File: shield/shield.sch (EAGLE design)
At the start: 23 parts, among them IC1 MCP2515-E/SO, IC2 MCP2551, IC3 LM2595NDH

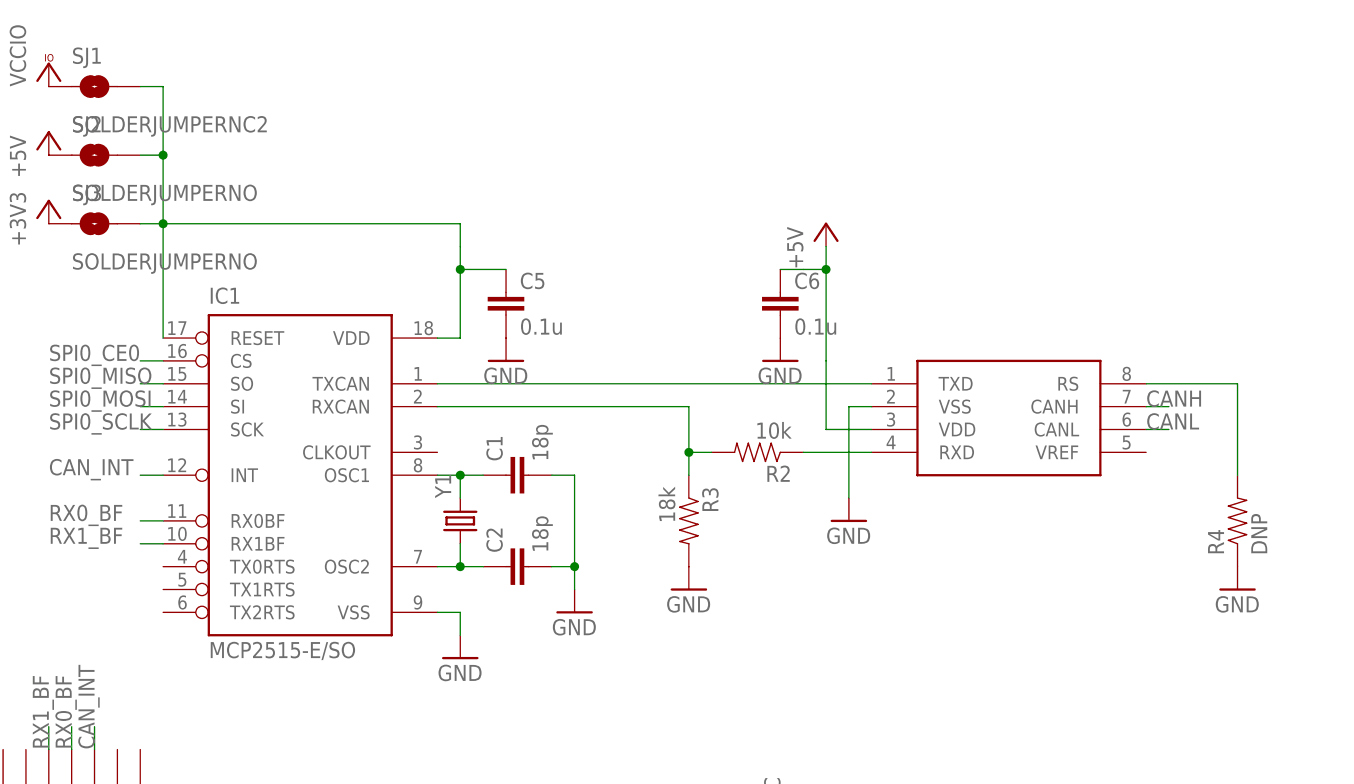
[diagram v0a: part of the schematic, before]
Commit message: Added power injector board; refactored boards to use MCP2562 instead of MCP2551
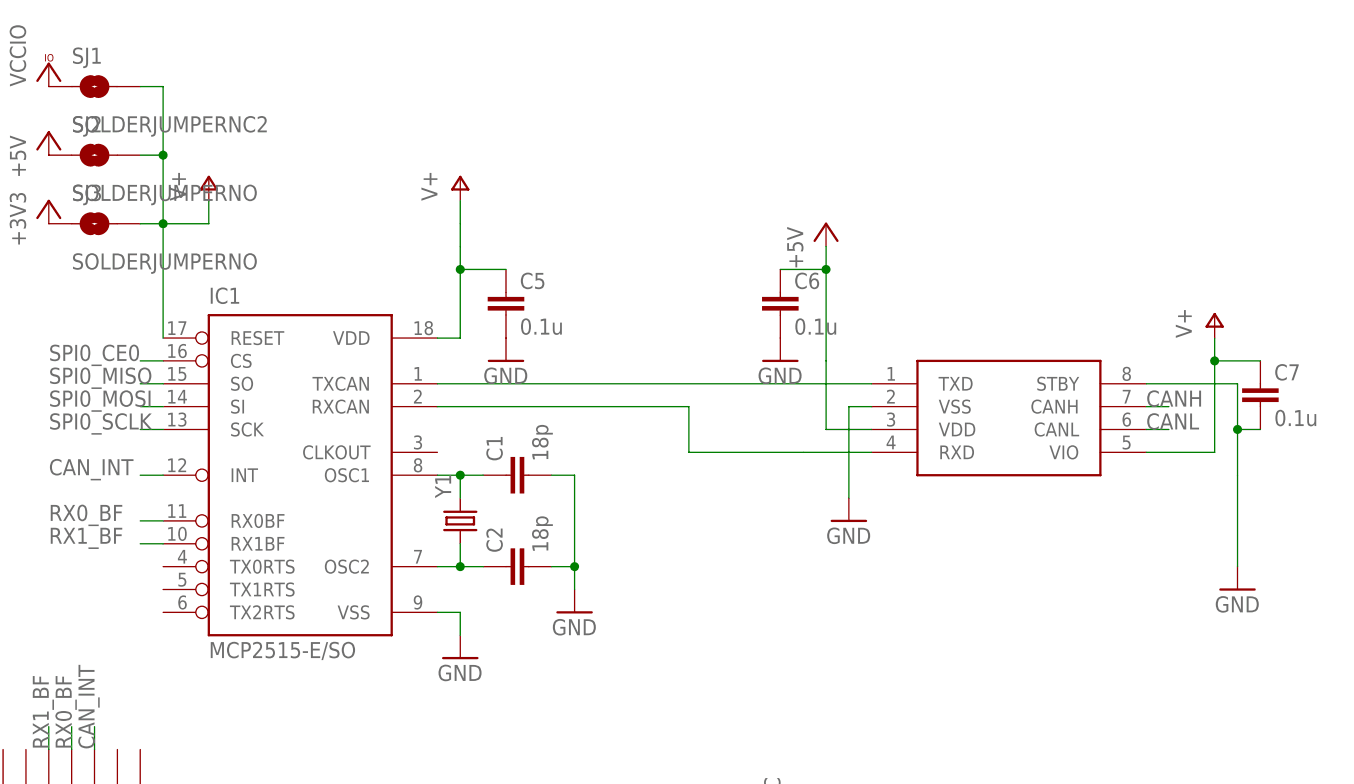
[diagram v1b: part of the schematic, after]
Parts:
- removed R2: 10k, SparkFun-Passives:RESISTOR0603-RES
- removed R3: 18k, SparkFun-Passives:RESISTOR0603-RES
- removed R4: DNP, SparkFun-Passives:RESISTOR0603-RES
- added C7: 0.1u, SparkFun-Passives:CAP0603-CAP
- IC2: value MCP2551 -> MCP2562; device SparkFun-DigitalIC:MCP2551 -> nickparts:MCP2562
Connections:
- removed net N$2: IC1.RXCAN, R2.2, R3.1
- removed net N$3: C5.1, IC1.RESET, IC1.VDD, SJ1.2, SJ2.2, SJ3.2
- removed net N$8: IC2.RS, R4.2
- new net V+: C5.1, C7.1, IC1.RESET, IC1.VDD, IC2.VIO, SJ1.2, SJ2.2, SJ3.2
- net GND: now also C7.2, IC2.STBY; no longer R3.2, R4.1
- net N$1: now also IC1.RXCAN; no longer R2.1
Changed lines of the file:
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@@
 <part name="D1" library="SparkFun-DiscreteSemi" deviceset="DIODE" device="SMA-ALT"/>
 <part name="IC1" library="mcp2515" deviceset="MCP2515" device="-E/SO"/>
-<part name="IC2" library="SparkFun-DigitalIC" deviceset="MCP2551" device=""/>
+<part name="IC2" library="nickparts" deviceset="MCP2562" device=""/>
 <part name="GND3" library="supply1" deviceset="GND" device=""/>
 <part name="P+1" library="supply1" deviceset="+5V" device=""/>
@@
 <part name="GND9" library="supply1" deviceset="GND" device=""/>
 <part name="GND10" library="supply1" deviceset="GND" device=""/>
-<part name="R4" library="SparkFun-Passives" deviceset="RESISTOR" device="0603-RES" value="DNP"/>
 <part name="GND11" library="supply1" deviceset="GND" device=""/>
 <part name="U$1" library="adafruit" deviceset="ARDUINO_R3_ICSP" device=""/>
@@
 <part name="VCC1" library="supply1" deviceset="VCCIO" device=""/>
 <part name="VCC3" library="supply1" deviceset="VCCIO" device=""/>
-<part name="R2" library="SparkFun-Passives" deviceset="RESISTOR" device="0603-RES" value="10k"/>
-<part name="R3" library="SparkFun-Passives" deviceset="RESISTOR" device="0603-RES" value="18k"/>
-<part name="GND1" library="supply1" deviceset="GND" device=""/>
 <part name="P+6" library="supply1" deviceset="+5V" device=""/>
 <part name="SJ1" library="SparkFun-Passives" deviceset="SOLDERJUMPER" device="NC2"/>
@@
 <part name="+3V1" library="supply1" deviceset="+3V3" device=""/>
 <part name="+3V2" library="supply1" deviceset="+3V3" device=""/>
+<part name="P+7" library="supply1" deviceset="V+" device=""/>
+<part name="P+8" library="supply1" deviceset="V+" device=""/>
+<part name="C7" library="SparkFun-Passives" deviceset="CAP" device="0603-CAP" value="0.1u"/>
+<part name="P+9" library="supply1" deviceset="V+" device=""/>
 </parts>
 <sheets>
@@
 <instance part="GND9" gate="1" x="368.3" y="-17.78"/>
 <instance part="GND10" gate="1" x="337.82" y="-17.78"/>
-<instance part="R4" gate="G$1" x="419.1" y="-35.56" rot="R90"/>
 <instance part="GND11" gate="1" x="419.1" y="-43.18"/>
 <instance part="U$1" gate="G$1" x="243.84" y="-116.84"/>
@@
 <instance part="VCC1" gate="G$1" x="259.08" y="-121.92"/>
 <instance part="VCC3" gate="G$1" x="287.02" y="15.24"/>
-<instance part="R2" gate="G$1" x="365.76" y="-27.94" rot="R180"/>
-<instance part="R3" gate="G$1" x="358.14" y="-35.56" rot="R270"/>
-<instance part="GND1" gate="1" x="358.14" y="-43.18"/>
 <instance part="P+6" gate="1" x="304.8" y="-83.82"/>
 <instance part="SJ1" gate="1" x="292.1" y="12.7"/>
@@
 <instance part="+3V1" gate="G$1" x="287.02" y="0"/>
 <instance part="+3V2" gate="G$1" x="251.46" y="-121.92"/>
+<instance part="P+7" gate="1" x="304.8" y="2.54"/>
+<instance part="P+8" gate="1" x="332.74" y="2.54"/>
+<instance part="C7" gate="G$1" x="421.64" y="-22.86"/>
+<instance part="P+9" gate="1" x="416.56" y="-12.7"/>
 </instances>
 <busses>
@@
 <pinref part="C5" gate="G$1" pin="2"/>
 <pinref part="GND10" gate="1" pin="GND"/>
-</segment>
-<segment>
-<pinref part="R4" gate="G$1" pin="1"/>
-<pinref part="GND11" gate="1" pin="GND"/>
 </segment>
 <segment>
@@
 </segment>
 <segment>
-<pinref part="R3" gate="G$1" pin="2"/>
-<pinref part="GND1" gate="1" pin="GND"/>
+<pinref part="IC2" gate="G$1" pin="STBY"/>
+<wire x1="408.94" y1="-20.32" x2="419.1" y2="-20.32" width="0.1524" layer="91"/>
+<wire x1="419.1" y1="-20.32" x2="419.1" y2="-25.4" width="0.1524" layer="91"/>
+<pinref part="GND11" gate="1" pin="GND"/>
+<wire x1="419.1" y1="-25.4" x2="419.1" y2="-30.48" width="0.1524" layer="91"/>
+<wire x1="419.1" y1="-30.48" x2="419.1" y2="-40.64" width="0.1524" layer="91"/>
+<pinref part="C7" gate="G$1" pin="2"/>
+<wire x1="421.64" y1="-25.4" x2="419.1" y2="-25.4" width="0.1524" layer="91"/>
+<junction x="419.1" y="-25.4"/>
 </segment>
 </net>
@@
 </segment>
 </net>
-<net name="N$8" class="0">
-<segment>
-<pinref part="IC2" gate="G$1" pin="RS"/>
-<pinref part="R4" gate="G$1" pin="2"/>
-<wire x1="408.94" y1="-20.32" x2="419.1" y2="-20.32" width="0.1524" layer="91"/>
-<wire x1="419.1" y1="-20.32" x2="419.1" y2="-30.48" width="0.1524" layer="91"/>
-</segment>
-</net>
 <net name="N$10" class="0">
 <segment>
@@
 <segment>
 <pinref part="IC2" gate="G$1" pin="RXD"/>
-<pinref part="R2" gate="G$1" pin="1"/>
 <wire x1="378.46" y1="-27.94" x2="370.84" y2="-27.94" width="0.1524" layer="91"/>
-</segment>
-</net>
-<net name="N$2" class="0">
-<segment>
-<pinref part="R2" gate="G$1" pin="2"/>
-<pinref part="R3" gate="G$1" pin="1"/>
-<wire x1="360.68" y1="-27.94" x2="358.14" y2="-27.94" width="0.1524" layer="91"/>
-<wire x1="358.14" y1="-27.94" x2="358.14" y2="-30.48" width="0.1524" layer="91"/>
 <pinref part="IC1" gate="G$1" pin="RXCAN"/>
 <wire x1="330.2" y1="-22.86" x2="358.14" y2="-22.86" width="0.1524" layer="91"/>
-<wire x1="358.14" y1="-22.86" x2="358.14" y2="-27.94" width="0.1524" layer="91"/>
-<junction x="358.14" y="-27.94"/>
-</segment>
-</net>
-<net name="N$3" class="0">
-<segment>
-<pinref part="IC1" gate="G$1" pin="VDD"/>
-<wire x1="330.2" y1="-15.24" x2="332.74" y2="-15.24" width="0.1524" layer="91"/>
-<wire x1="332.74" y1="-15.24" x2="332.74" y2="-7.62" width="0.1524" layer="91"/>
-<pinref part="C5" gate="G$1" pin="1"/>
-<wire x1="337.82" y1="-7.62" x2="332.74" y2="-7.62" width="0.1524" layer="91"/>
-<wire x1="332.74" y1="-7.62" x2="332.74" y2="-5.08" width="0.1524" layer="91"/>
-<junction x="332.74" y="-7.62"/>
-<wire x1="332.74" y1="-5.08" x2="332.74" y2="-2.54" width="0.1524" layer="91"/>
+<wire x1="370.84" y1="-27.94" x2="358.14" y2="-27.94" width="0.1524" layer="91"/>
+<wire x1="358.14" y1="-27.94" x2="358.14" y2="-22.86" width="0.1524" layer="91"/>
+</segment>
+</net>
+<net name="+3V3" class="0">
+<segment>
+<pinref part="SJ3" gate="1" pin="1"/>
+<pinref part="+3V1" gate="G$1" pin="+3V3"/>
+</segment>
+<segment>
+<pinref part="U$1" gate="G$1" pin="3V"/>
+<wire x1="271.78" y1="-121.92" x2="271.78" y2="-129.54" width="0.1524" layer="91"/>
+<pinref part="+3V2" gate="G$1" pin="+3V3"/>
+<wire x1="271.78" y1="-129.54" x2="251.46" y2="-129.54" width="0.1524" layer="91"/>
+<wire x1="251.46" y1="-129.54" x2="251.46" y2="-124.46" width="0.1524" layer="91"/>
+</segment>
+</net>
+<net name="V+" class="0">
+<segment>
 <pinref part="SJ1" gate="1" pin="2"/>
 <wire x1="297.18" y1="12.7" x2="299.72" y2="12.7" width="0.1524" layer="91"/>
@@
 <wire x1="297.18" y1="5.08" x2="299.72" y2="5.08" width="0.1524" layer="91"/>
 <junction x="299.72" y="5.08"/>
-<wire x1="332.74" y1="-2.54" x2="299.72" y2="-2.54" width="0.1524" layer="91"/>
 <junction x="299.72" y="-2.54"/>
 <pinref part="IC1" gate="G$1" pin="RESET"/>
 <wire x1="299.72" y1="-2.54" x2="299.72" y2="-15.24" width="0.1524" layer="91"/>
-</segment>
-</net>
-<net name="+3V3" class="0">
-<segment>
-<pinref part="SJ3" gate="1" pin="1"/>
-<pinref part="+3V1" gate="G$1" pin="+3V3"/>
-</segment>
-<segment>
-<pinref part="U$1" gate="G$1" pin="3V"/>
-<wire x1="271.78" y1="-121.92" x2="271.78" y2="-129.54" width="0.1524" layer="91"/>
-<pinref part="+3V2" gate="G$1" pin="+3V3"/>
-<wire x1="271.78" y1="-129.54" x2="251.46" y2="-129.54" width="0.1524" layer="91"/>
-<wire x1="251.46" y1="-129.54" x2="251.46" y2="-124.46" width="0.1524" layer="91"/>
-</segment>
-</net>
+<pinref part="P+7" gate="1" pin="V+"/>
+<wire x1="299.72" y1="-2.54" x2="304.8" y2="-2.54" width="0.1524" layer="91"/>
+<wire x1="304.8" y1="-2.54" x2="304.8" y2="0" width="0.1524" layer="91"/>
+</segment>
+<segment>
+<wire x1="332.74" y1="-5.08" x2="332.74" y2="-2.54" width="0.1524" layer="91"/>
+<pinref part="C5" gate="G$1" pin="1"/>
+<wire x1="337.82" y1="-7.62" x2="332.74" y2="-7.62" width="0.1524" layer="91"/>
+<wire x1="332.74" y1="-7.62" x2="332.74" y2="-5.08" width="0.1524" layer="91"/>
+<junction x="332.74" y="-7.62"/>
+<wire x1="332.74" y1="-15.24" x2="332.74" y2="-7.62" width="0.1524" layer="91"/>
+<pinref part="IC1" gate="G$1" pin="VDD"/>
+<wire x1="330.2" y1="-15.24" x2="332.74" y2="-15.24" width="0.1524" layer="91"/>
+<pinref part="P+8" gate="1" pin="V+"/>
+<wire x1="332.74" y1="0" x2="332.74" y2="-2.54" width="0.1524" layer="91"/>
+</segment>
+<segment>
+<pinref part="IC2" gate="G$1" pin="VIO"/>
+<wire x1="408.94" y1="-27.94" x2="416.56" y2="-27.94" width="0.1524" layer="91"/>
+<wire x1="416.56" y1="-27.94" x2="416.56" y2="-17.78" width="0.1524" layer="91"/>
+<pinref part="C7" gate="G$1" pin="1"/>
+<wire x1="416.56" y1="-17.78" x2="416.56" y2="-15.24" width="0.1524" layer="91"/>
+<wire x1="421.64" y1="-17.78" x2="416.56" y2="-17.78" width="0.1524" layer="91"/>
+<junction x="416.56" y="-17.78"/>
+<pinref part="P+9" gate="1" pin="V+"/>
+</segment>
+</net>

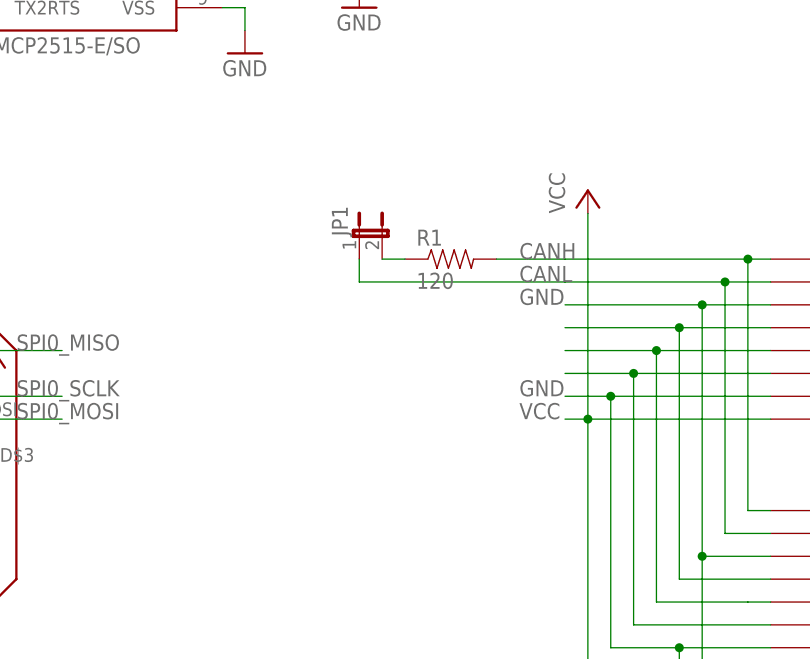
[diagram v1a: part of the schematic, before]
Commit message: Switch to split termination with a switch
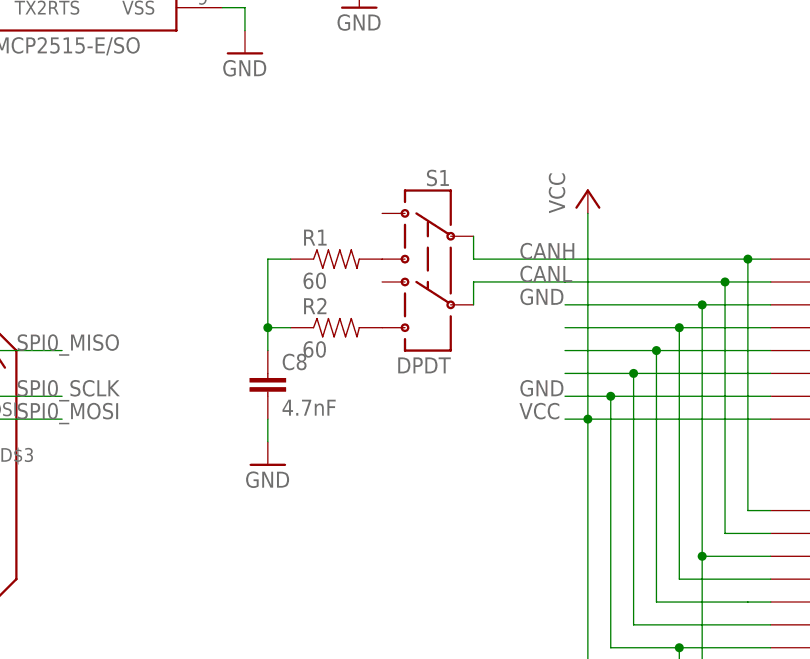
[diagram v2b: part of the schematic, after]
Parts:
- removed JP1: (no value), SparkFun-Passives:JUMPER-2PTH
- added C8: 4.7nF, SparkFun-Passives:CAP0603-CAP
- added R2: 60, SparkFun-Passives:RESISTOR0603-RES
- added S1: DPDT, SparkFun-Electromechanical:SWITCH-DPDTAYZ0202
- R1: value 120 -> 60
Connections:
- new net N$2: R1.2, S1.3
- new net N$3: R2.2, S1.6
- net CANH: now also S1.2; no longer R1.2
- net CANL: now also S1.5; no longer JP1.1
- net GND: now also C8.2
- net N$7: now also C8.1, R2.1; no longer JP1.2
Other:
- moved on the sheet: R1
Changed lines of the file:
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@@
 <part name="GND8" library="supply1" deviceset="GND" device=""/>
 <part name="P+5" library="supply1" deviceset="VCC" device=""/>
-<part name="JP1" library="SparkFun-Passives" deviceset="JUMPER-2" device="PTH"/>
-<part name="R1" library="SparkFun-Passives" deviceset="RESISTOR" device="0603-RES" value="120"/>
+<part name="R1" library="SparkFun-Passives" deviceset="RESISTOR" device="0603-RES" value="60"/>
 <part name="VCC1" library="supply1" deviceset="VCCIO" device=""/>
 <part name="VCC3" library="supply1" deviceset="VCCIO" device=""/>
@@
 <part name="C7" library="SparkFun-Passives" deviceset="CAP" device="0603-CAP" value="0.1u"/>
 <part name="P+9" library="supply1" deviceset="V+" device=""/>
+<part name="S1" library="SparkFun-Electromechanical" deviceset="SWITCH-DPDT" device="AYZ0202" value="DPDT"/>
+<part name="R2" library="SparkFun-Passives" deviceset="RESISTOR" device="0603-RES" value="60"/>
+<part name="C8" library="SparkFun-Passives" deviceset="CAP" device="0603-CAP" value="4.7nF"/>
+<part name="GND1" library="supply1" deviceset="GND" device=""/>
 </parts>
 <sheets>
@@
 <instance part="GND8" gate="1" x="383.54" y="-127"/>
 <instance part="P+5" gate="VCC" x="370.84" y="-66.04"/>
-<instance part="JP1" gate="A" x="345.44" y="-71.12"/>
-<instance part="R1" gate="G$1" x="355.6" y="-73.66"/>
+<instance part="R1" gate="G$1" x="342.9" y="-73.66"/>
 <instance part="VCC1" gate="G$1" x="259.08" y="-121.92"/>
 <instance part="VCC3" gate="G$1" x="287.02" y="15.24"/>
@@
 <instance part="C7" gate="G$1" x="421.64" y="-22.86"/>
 <instance part="P+9" gate="1" x="416.56" y="-12.7"/>
+<instance part="S1" gate="G$1" x="353.06" y="-73.66" rot="MR0"/>
+<instance part="R2" gate="G$1" x="342.9" y="-81.28"/>
+<instance part="C8" gate="G$1" x="335.28" y="-88.9"/>
+<instance part="GND1" gate="1" x="335.28" y="-96.52"/>
 </instances>
 <busses>
@@
 <junction x="419.1" y="-25.4"/>
 </segment>
+<segment>
+<pinref part="C8" gate="G$1" pin="2"/>
+<pinref part="GND1" gate="1" pin="GND"/>
+<wire x1="335.28" y1="-91.44" x2="335.28" y2="-93.98" width="0.1524" layer="91"/>
+</segment>
 </net>
 <net name="N$6" class="0">
@@
 <junction x="388.62" y="-73.66"/>
 <label x="363.22" y="-73.66" size="1.778" layer="95"/>
-<pinref part="R1" gate="G$1" pin="2"/>
-<wire x1="368.3" y1="-73.66" x2="360.68" y2="-73.66" width="0.1524" layer="91"/>
+<pinref part="S1" gate="G$1" pin="2"/>
+<wire x1="368.3" y1="-73.66" x2="358.14" y2="-73.66" width="0.1524" layer="91"/>
+<wire x1="358.14" y1="-73.66" x2="358.14" y2="-71.12" width="0.1524" layer="91"/>
 </segment>
 </net>
@@
 <junction x="386.08" y="-76.2"/>
 <label x="363.22" y="-76.2" size="1.778" layer="95"/>
-<pinref part="JP1" gate="A" pin="1"/>
-<wire x1="368.3" y1="-76.2" x2="345.44" y2="-76.2" width="0.1524" layer="91"/>
-<wire x1="345.44" y1="-76.2" x2="345.44" y2="-73.66" width="0.1524" layer="91"/>
+<pinref part="S1" gate="G$1" pin="5"/>
+<wire x1="368.3" y1="-76.2" x2="358.14" y2="-76.2" width="0.1524" layer="91"/>
+<wire x1="358.14" y1="-76.2" x2="358.14" y2="-78.74" width="0.1524" layer="91"/>
 </segment>
 </net>
@@
 <wire x1="375.92" y1="-86.36" x2="368.3" y2="-86.36" width="0.1524" layer="91"/>
 <junction x="375.92" y="-86.36"/>
-</segment>
-</net>
-<net name="N$7" class="0">
-<segment>
-<pinref part="JP1" gate="A" pin="2"/>
-<pinref part="R1" gate="G$1" pin="1"/>
-<wire x1="347.98" y1="-73.66" x2="350.52" y2="-73.66" width="0.1524" layer="91"/>
 </segment>
 </net>
@@
 </segment>
 </net>
+<net name="N$7" class="0">
+<segment>
+<pinref part="R1" gate="G$1" pin="1"/>
+<pinref part="C8" gate="G$1" pin="1"/>
+<wire x1="337.82" y1="-73.66" x2="335.28" y2="-73.66" width="0.1524" layer="91"/>
+<wire x1="335.28" y1="-73.66" x2="335.28" y2="-81.28" width="0.1524" layer="91"/>
+<pinref part="R2" gate="G$1" pin="1"/>
+<wire x1="335.28" y1="-81.28" x2="335.28" y2="-83.82" width="0.1524" layer="91"/>
+<wire x1="337.82" y1="-81.28" x2="335.28" y2="-81.28" width="0.1524" layer="91"/>
+<junction x="335.28" y="-81.28"/>
+</segment>
+</net>
+<net name="N$2" class="0">
+<segment>
+<pinref part="S1" gate="G$1" pin="3"/>
+<pinref part="R1" gate="G$1" pin="2"/>
+</segment>
+</net>
+<net name="N$3" class="0">
+<segment>
+<pinref part="S1" gate="G$1" pin="6"/>
+<pinref part="R2" gate="G$1" pin="2"/>
+</segment>
+</net>
